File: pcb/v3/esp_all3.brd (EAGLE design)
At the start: 45 x 95 mm, 25 parts, among them Q1 BUZ11BH

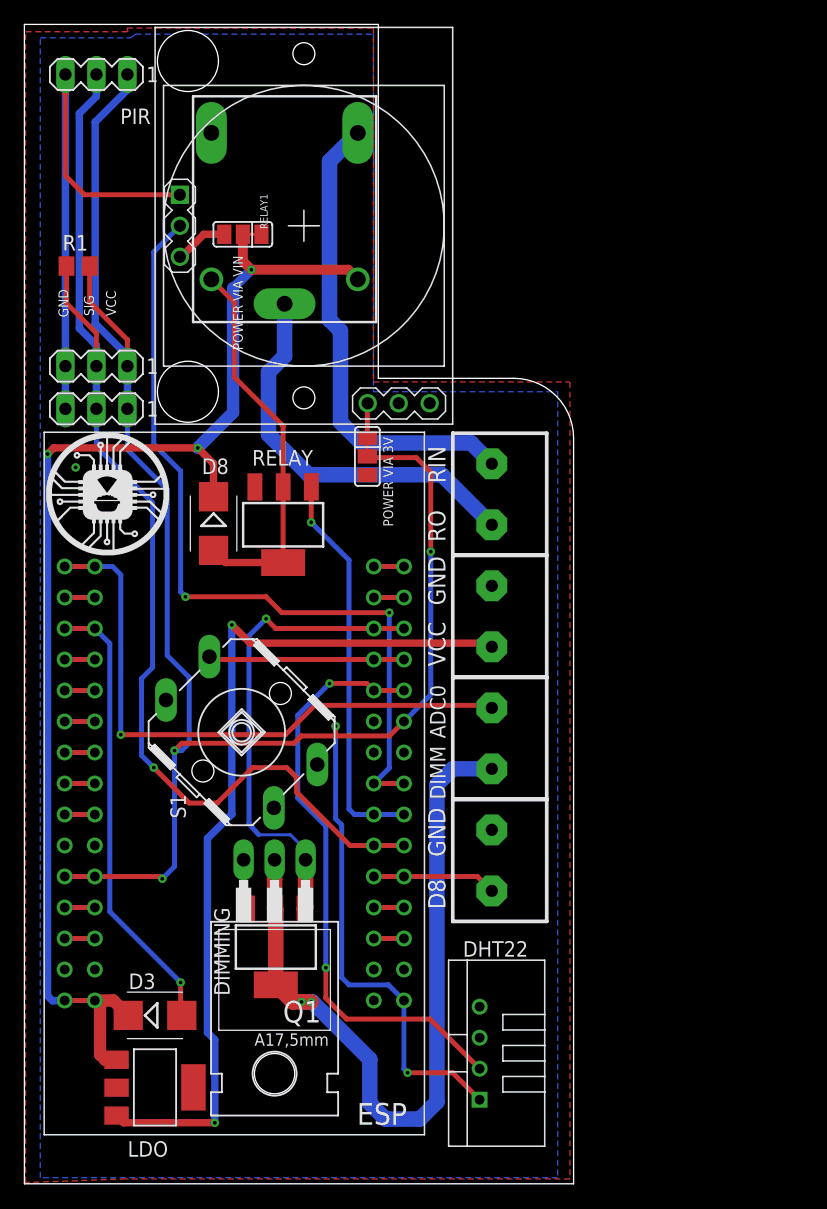
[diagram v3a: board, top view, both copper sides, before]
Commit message: flipped PIR
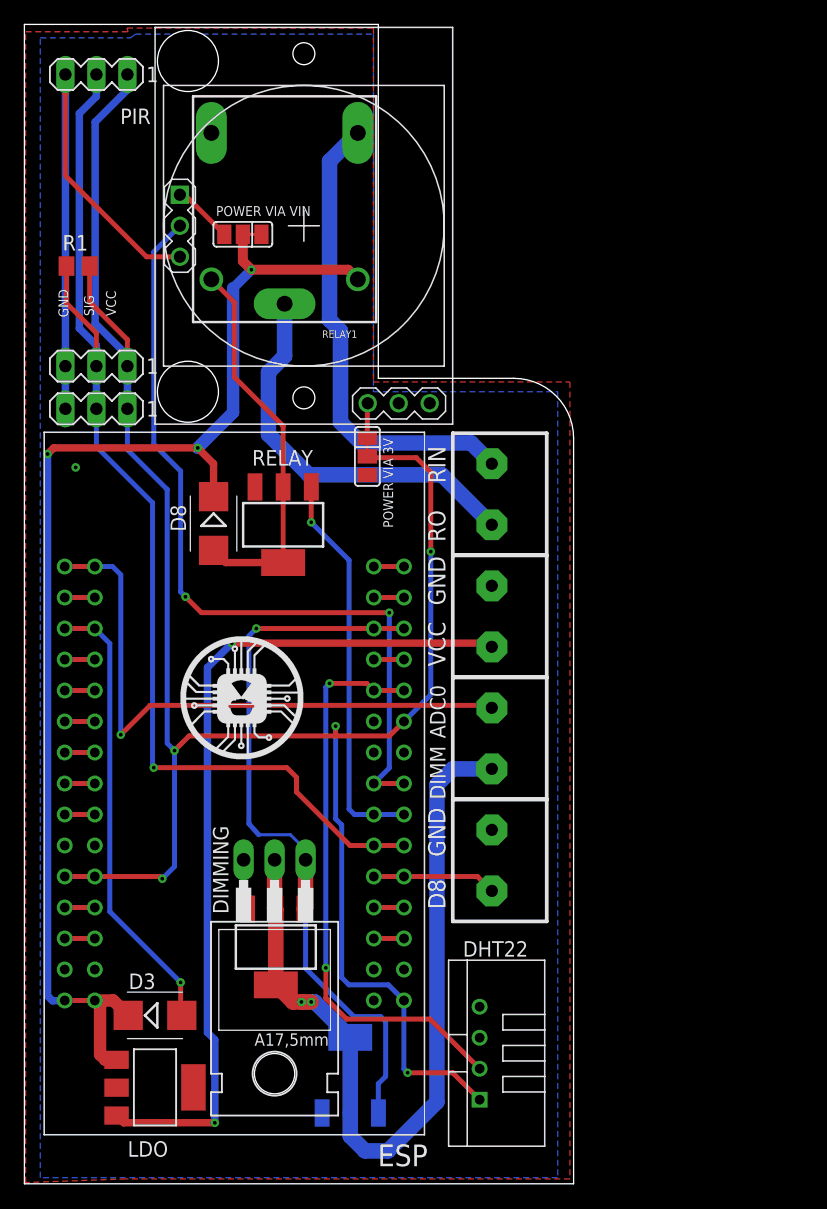
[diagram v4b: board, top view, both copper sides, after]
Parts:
- removed S1: (no value), switch-omron:B3F/40XX
- added DIMMING2: DMN6068SE-13, transistor-power:SOT223
- moved U$11 20.0 mm to (12.8, 34.8)
- moved U$9 17.4 mm to (44.4, 8.70)
- moved U$4 9.00 mm to (44.2, 1.10)
- moved U$1 3.00 mm to (18.7, 14.4)
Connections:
- net DIMMING: now also DIMMING2.2, DIMMING2.4
- net GND: now also DIMMING2.3, PIR.3; no longer PIR.1, S1.3, S1.4
- net N$27: no longer S1.1
- net N$31: now also PIR.1; no longer PIR.3
- net TTL_DIMM: now also DIMMING2.1
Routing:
- net TTL_DIMM: track 39.5 -> 63.8 mm
- net N$27: track 16.0 -> 2.47 mm
- net DIMMING: track 62.8 -> 67.7 mm
- net N$15: track 96.6 -> 93.5 mm
- net N$17: track 72.2 -> 70.1 mm
- net GND: track 47.1 -> 49.2 mm
- net DHT_SIG: track 49.2 -> 47.3 mm
- net 3V3: track 176.2 -> 174.9 mm
- net N$31: track 4.45 -> 4.98 mm

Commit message: added more transistors
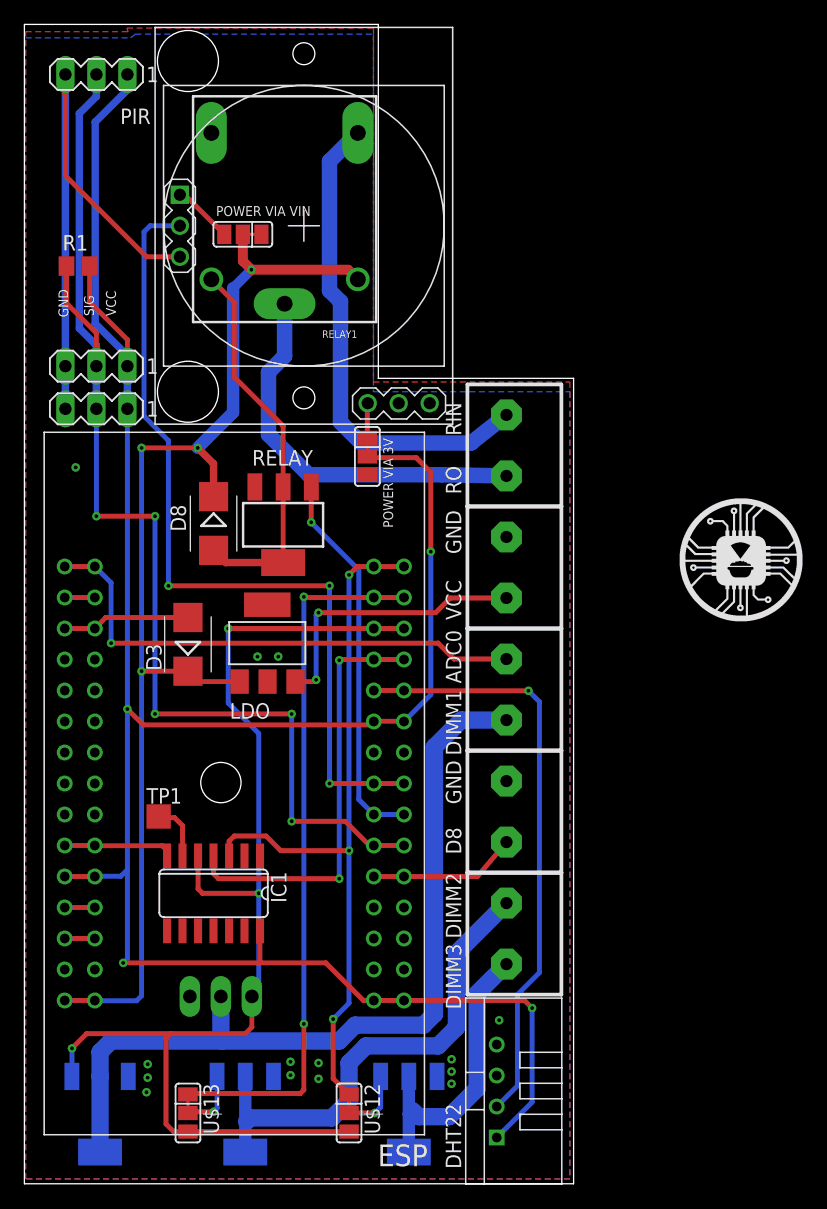
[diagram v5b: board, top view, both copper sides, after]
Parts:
- added DIMMING1: DMN6068SE-13, transistor-power:SOT223
- added IC1: 4000D, 40xx:SO14
- added TP1: TPTP20SQ, testpad:TP20SQ
- added U$12, U$13: SMD_SJ_3WAY_CLOSED, JKW_CHIP:SMD_SJ_3WAY_CLOSED
- added U$2: V1, JKW_CHIP:2_SCREW_PIN
- moved U$11 42.4 mm to (53.7, 46.1)
- moved U$1 42.4 mm to (61.1, 15.9)
- moved LDO 37.5 mm to (19.9, 44.3), turned to 0 degrees
- moved D3 30.5 mm to (13.4, 44.2), turned to 90 degrees
- moved DIMMING 19.9 mm to (6.20, 5.70), flipped to the bottom
- moved DIMMING2 5.77 mm to (31.5, 5.70), turned to 180 degrees
- moved Q1 4.65 mm to (16.1, 21.7), flipped to the bottom, turned to 0 degrees
- moved U$10 4.18 mm to (40.0, 30.5)
- moved U$3 4.18 mm to (40.0, 40.5)
- moved U$7 4.18 mm to (40.0, 50.5)
- moved U$8 4.18 mm to (40.0, 60.5)
- moved DHT22 3.40 mm to (38.7, 7.60)
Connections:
- net N$10 renamed RERLAY
- net N$15 renamed ONEWIRE_DS12B20
- removed net 3V3: DHT22.1, ESP.3V3@0, ESP.3V3@3, ESP.3V3@4, ESP.3V3@5, R1.2, SV1.1, SV2.1, SV3.1, U$5.2
- removed net DIMMING: DIMMING.2, DIMMING.4, DIMMING2.2, DIMMING2.4, Q1.D, U$3.P$1
- removed net N$11: ESP.3V3@2
- removed net N$16: ESP.D1, ESP.D11
- removed net N$18: ESP.TX, ESP.TX1
- removed net N$19: ESP.RX, ESP.RX1
- removed net N$27: ESP.D3, ESP.D31
- removed net N$3: ESP.3V3@1
- removed net N$30: ESP.D0, ESP.D01
- removed net N$5: ESP.SD2, ESP.SD22
- removed net N$6: ESP.SD1, ESP.SD12
- removed net N$7: ESP.CMD, ESP.CMD1
- removed net N$8: ESP.SD0, ESP.SD01
- removed net N$9: ESP.CLK, ESP.CLK1
- removed net TTL_DIMM: DIMMING.1, DIMMING2.1, ESP.D2, ESP.D21, Q1.G
- new net DIMM1: DIMMING.1, ESP.D2, ESP.D21, IC1.5, Q1.G, U$12.3, U$13.3
- new net DIMM2: ESP.D1, ESP.D11, U$13.1
- new net DIMM3: ESP.D0, ESP.D01, IC1.3, U$12.1
- new net DIMMING1: DIMMING.2, DIMMING.4, Q1.D, U$3.P$1
- new net DIMMING2: DIMMING1.2, DIMMING1.4, U$2.P$2
- new net DIMMING3: DIMMING2.2, DIMMING2.4, U$2.P$1
- new net N$20: DIMMING2.1, U$12.2
- new net N$21: DIMMING1.1, U$13.2
- new net NOT: ESP.D3, ESP.D31, IC1.4
- new net VDD: DHT22.1, ESP.3V3@0, ESP.3V3@1, ESP.3V3@2, ESP.3V3@3, ESP.3V3@4, ESP.3V3@5, IC1.14, R1.2, SV1.1, SV2.1, SV3.1, U$5.2
- net GND: now also DIMMING1.3, IC1.7
- net N$4: now also IC1.6, TP1.TP; no longer ESP.SD3, ESP.SD32
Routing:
- net VDD: track 0.00 -> 189.9 mm, vias 0 -> 4
- net 3V3: track 174.9 -> 0.00 mm, vias 5 -> 0
- net DIMM1: track 0.00 -> 96.7 mm, vias 0 -> 3
- net DIMMING1: track 0.00 -> 69.3 mm
- net DIMMING: track 67.7 -> 0.00 mm, vias 2 -> 0
- net TTL_DIMM: track 63.8 -> 0.00 mm, vias 1 -> 0
- net DIMM3: track 0.00 -> 60.2 mm, vias 0 -> 3
- net DIMM2: track 0.00 -> 58.3 mm, vias 0 -> 2
- net N$17: track 70.1 -> 23.2 mm
- net DIMMING2: track 0.00 -> 40.4 mm
- net NOT: track 0.00 -> 35.2 mm, vias 0 -> 2
- net N$14: track 37.1 -> 10.5 mm, vias 1 -> 0
- net DIMMING3: track 0.00 -> 24.3 mm
- net GND: track 49.2 -> 58.2 mm, vias 1 -> 14
- net N$1: track 49.5 -> 42.2 mm
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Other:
- outline, holes or cut-outs redrawn
- board text added: "DIMM1"
- board text added: "DIMM2"
- board text added: "DIMM3"

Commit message: added jumper
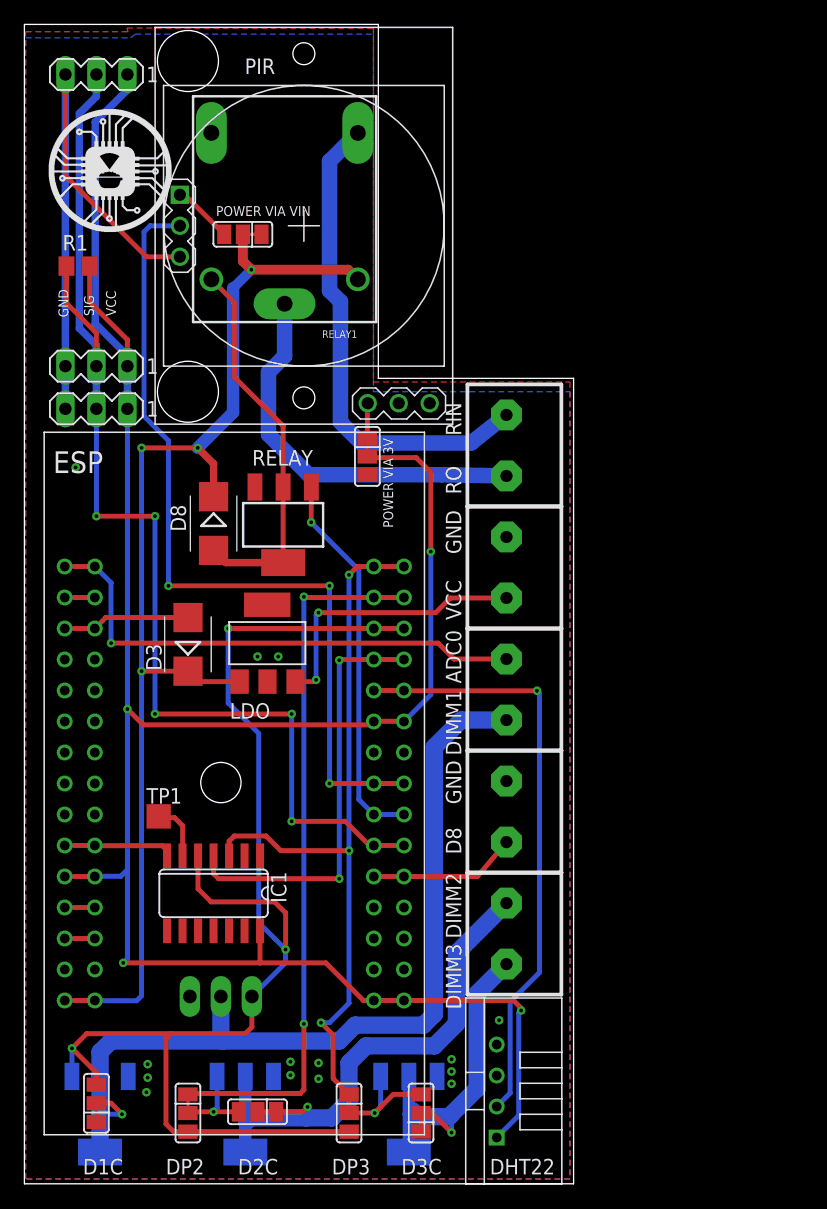
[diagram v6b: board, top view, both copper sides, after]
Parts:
- added D1C, D2C, D3C: SMD_SJ_3WAY_CLOSED, JKW_CHIP:SMD_SJ_3WAY_CLOSED
- moved U$11 60.7 mm to (2.00, 78.0)
- moved U$1 45.7 mm to (22.9, 41.0)
- renumbered U$12 to DP3, U$13 to DP2
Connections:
- net DIMM1: now also D1C.3
- net DIMMING1: now also D1C.2
- net DIMMING2: now also D2C.2
- net DIMMING3: now also D3C.2
- net N$20: now also D3C.3
- net N$21: now also D2C.3
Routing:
- net DIMM1: track 96.7 -> 108.2 mm
- net DIMMING2: track 40.4 -> 45.5 mm, vias 0 -> 1
- net DIMMING3: track 24.3 -> 28.9 mm, vias 0 -> 1
- net N$20: track 5.30 -> 9.73 mm
- net DIMMING1: track 69.3 -> 73.6 mm, vias 0 -> 1
- net N$21: track 5.16 -> 7.24 mm
- net VDD: track 189.9 -> 188.6 mm
- net DIMM3: track 60.2 -> 61.5 mm

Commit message: added v4, with i2c
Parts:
- removed D1C, D2C, D3C: SMD_SJ_3WAY_CLOSED, JKW_CHIP:SMD_SJ_3WAY_CLOSED
- added R2, R3: 4.7k, rcl:M0805
- moved U$4 87.0 mm to (9.10, 80.7)
- moved U$9 72.9 mm to (8.90, 72.4)
- moved U$1 12.1 mm to (24.1, 53.0)
- renumbered DIMMING to T_DIM1, DIMMING1 to T_DIM2, DIMMING2 to T_DIM3
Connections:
- new net N$3: R2.2, R3.2, T_DIM3.2, T_DIM3.4
- net DIMM1: no longer D1C.3
- net DIMMING1: no longer D1C.2
- net DIMMING2: no longer D2C.2
- net DIMMING3: now also R3.1; no longer D3C.2, T_DIM3.2, T_DIM3.4
- net GND: now also R2.1
- net N$20: no longer D3C.3
- net N$21: no longer D2C.3
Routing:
- net N$3: track 0.00 -> 20.7 mm, vias 0 -> 1
- net DIMMING3: track 28.9 -> 8.45 mm, vias 1 -> 0
- net DIMMING2: track 45.5 -> 40.4 mm, vias 1 -> 0
- net N$20: track 9.73 -> 5.30 mm
- net DIMMING1: track 73.6 -> 69.3 mm, vias 1 -> 0
- net DIMM1: track 108.2 -> 104.4 mm
- net N$21: track 7.24 -> 5.16 mm
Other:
- board text added: "DIM1"
- board text added: "DIM2"
- board text added: "DIM3"
- board text removed: "DIMM1"
